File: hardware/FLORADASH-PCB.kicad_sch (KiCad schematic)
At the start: 45 parts, among them IC1 LM66200DRLR, J1 USB_C_Receptacle_USB2.0_16P, Q1 FS8205, Q2 FS8205, U1 ESP32-C3-WROOM-02, U2 TP4056-42-ESOP8, U3 USBLC6-2SC6, U5 MAX17048G_T10, U6 DW01A

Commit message: Added the DHT11 Module
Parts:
- added U7: DHT11, Connector_PinSocket_2.54mm:PinSocket_1x03_P2.54mm_Vertical, symbol DHT11_Board:DHT11_Board
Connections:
- net +3.3V: now also U7.2 (VCC)
- net GND: now also U7.3 (GND)

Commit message: New labels
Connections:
- net B+ is gone; now on net Bat+: BT1.1 (+), C4.1, IC1.6 (VIN2), R9.1, TP5.1, U2.5 (BAT)
- net B_Or_USB is gone; now on net battery/usb: IC1.2 (VOUT@1), IC1.7 (VOUT@2), TP3.1
- net B- renamed Bat-
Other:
- note added: "Sensor Humidity / Temperature"
- moved on the sheet: BT1, C3, C4, C9, D3, Q1, Q2, R10, R5, R6, R9, TP5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

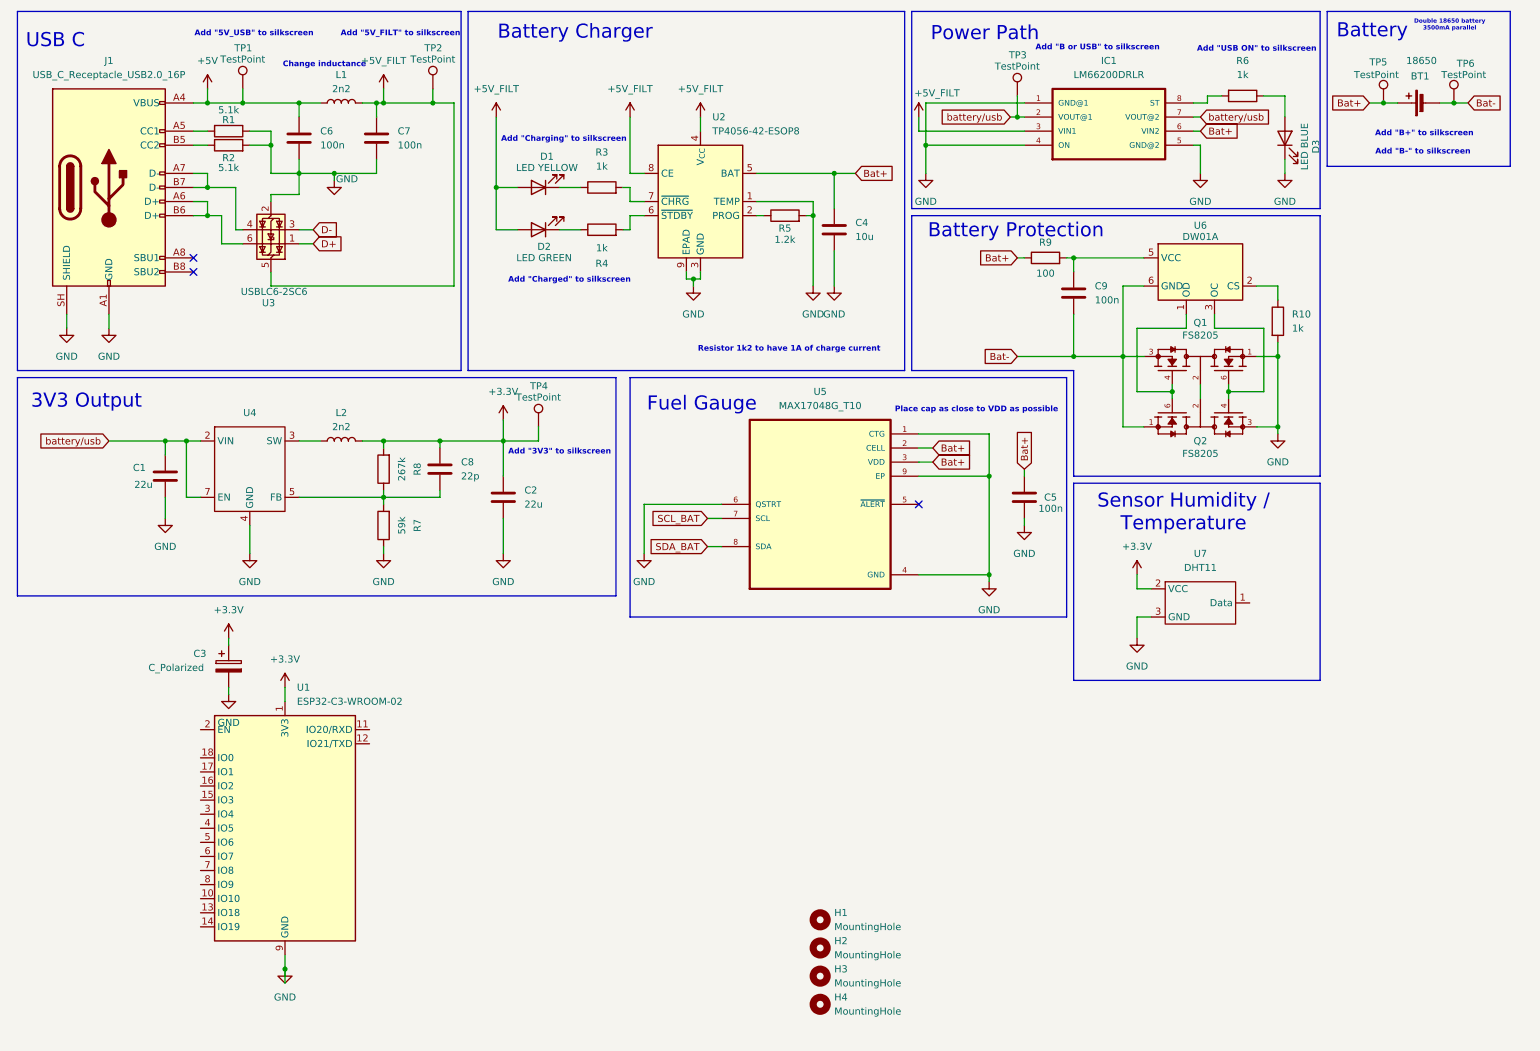
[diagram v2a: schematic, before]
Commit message: Added the Soil Moisture Sensor and LDR Sensor
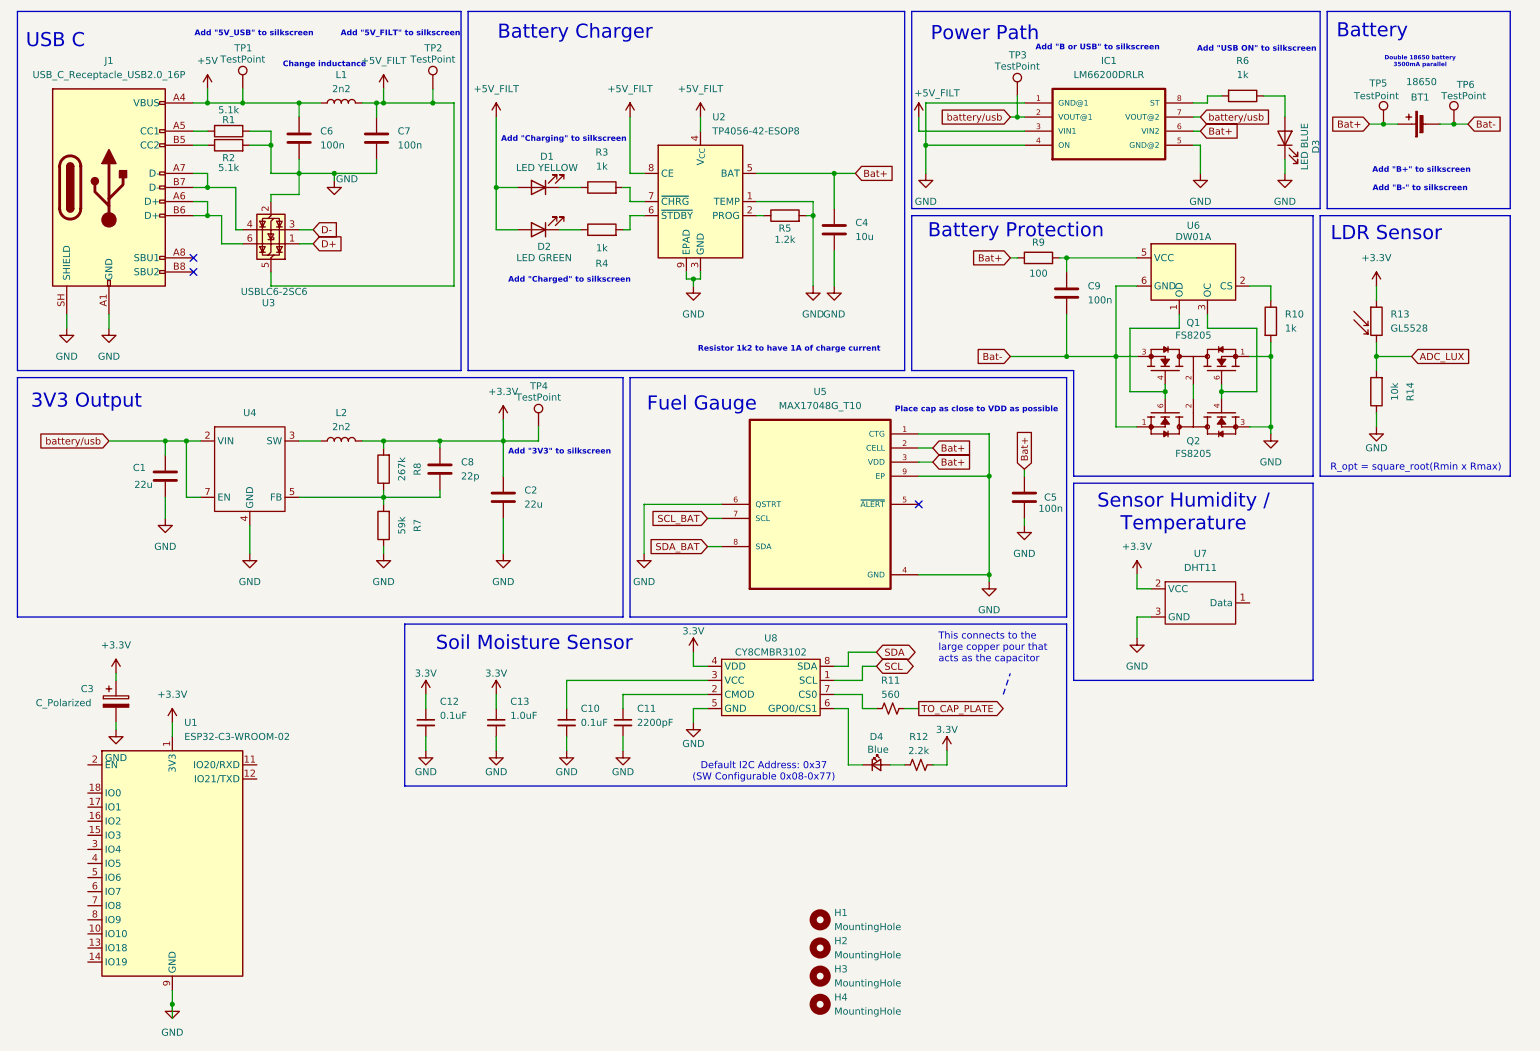
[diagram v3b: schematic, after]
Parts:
- added C10, C12: 0.1uF, SparkFun-Capacitor:C_0603_1608Metric, symbol SparkFun-Capacitor:0.1uF_0603_25V_20%
- added C11: 2200pF, SparkFun-Capacitor:C_0603_1608Metric, symbol SparkFun-Capacitor:2200pF_0603_50V_10%
- added C13: 1.0uF, SparkFun-Capacitor:C_0603_1608Metric, symbol SparkFun-Capacitor:1.0uF_0603_16V_10%
- added D4: Blue, SparkFun-LED:LED_0603_1608Metric_Blue, symbol SparkFun-LED:LED_Blue_0603
- added R11: 560, SparkFun-Resistor:R_0603_1608Metric, symbol SparkFun-Resistor:560_0603
- added R12: 2.2k, SparkFun-Resistor:R_0603_1608Metric, symbol SparkFun-Resistor:2.2k_0603
- added R13: GL5528, Connector_PinSocket_2.00mm:PinSocket_1x02_P2.00mm_Vertical, symbol Device:R_Photo
- added R14: 10k, symbol Device:R
- added U8: CY8CMBR3102, SparkFun-Semiconductor-Standard:SO-8, symbol SparkFun-Sensor:CY8CMBR3102
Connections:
- net +3.3V: now also R13.1
- net GND: now also C10.2, C11.2, C12.2, C13.2, R14.1, U8.5 (GND)
- new net: C11.1, U8.2 (CMOD)
- new net: C10.1, U8.3 (VCC)
- new net: D4.1 (K), U8.6 (GPO0/CS1)
- new net: R11.1, U8.7 (CS0)
- new net: D4.2 (A), R12.2
- new net 3.3V: C12.1, C13.1, R12.1, U8.4 (VDD)
- new net ADC_LUX: R13.2, R14.2
- new net SCL: U8.1 (SCL)
- new net SDA: U8.8 (SDA)
- new net TO_CAP_PLATE: R11.2
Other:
- note added: "Default I2C Address: 0x37 (SW Configurable 0x08-0x77)"
- note added: "LDR Sensor"
- note added: "R_opt = square_root(Rmin x Rmax)"
- note added: "Soil Moisture Sensor"
- note added: "This connects to the large copper pour that acts as the capacitor"
- moved on the sheet: BT1, C3, C9, Q1, Q2, R10, R9, TP5, TP6, U1, U6

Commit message: Added the Switch and low pass filter
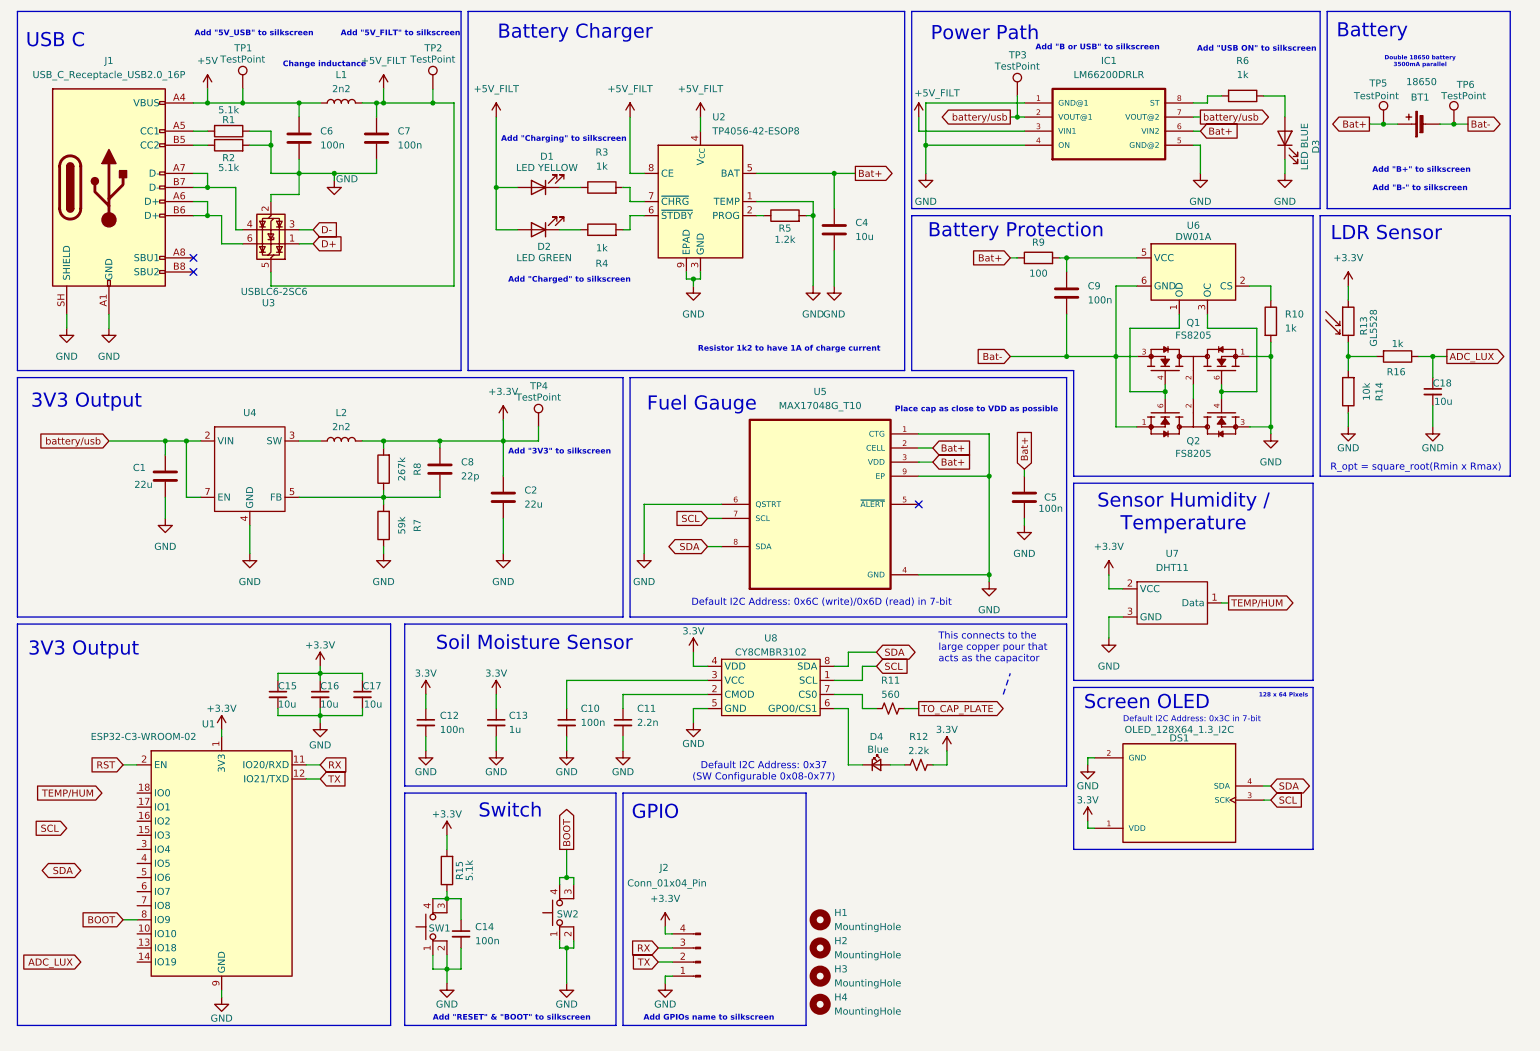
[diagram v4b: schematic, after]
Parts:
- removed C3: C_Polarized, symbol Device:C_Polarized
- added C14: 100n, SparkFun-Capacitor:C_0603_1608Metric, symbol SparkFun-Capacitor:0.1uF_0603_25V_20%
- added C15, C16, C17, C18: 10u, SparkFun-Capacitor:C_0603_1608Metric, symbol SparkFun-Capacitor:1.0uF_0603_16V_10%
- added DS1: OLED_128X64_1.3_I2C, OLED_128X64_1.3_I2C:LCD_OLED_128X64_1.3_I2C, symbol OLED_128X64_1.3_I2C:OLED_128X64_1.3_I2C
- added J2: Conn_01x04_Pin, symbol Connector:Conn_01x04_Pin
- added R15: 5.1k, symbol Device:R
- added R16: 1k, symbol Device:R
- added SW1: RESET, symbol Switch:SW_MEC_5E
- added SW2: BOOT, symbol Switch:SW_MEC_5E
- C10, C12: value 0.1uF -> 100n
- C11: value 2200pF -> 2.2n
- C13: value 1.0uF -> 1u
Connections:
- net SCL_BAT is gone; now on net SCL: U5.7 (SCL)
- net SDA_BAT is gone; now on net SDA: U5.8 (SDA)
- net +3.3V: now also C15.1, C16.1, C17.1, J2.4 (Pin_4), R15.2
- net 3.3V: now also DS1.1 (VDD)
- net ADC_LUX: now also C18.1, R16.1; no longer R13.2, R14.2
- net GND: now also C14.2, C15.2, C16.2, C17.2, C18.2, DS1.2 (GND), J2.1 (Pin_1), SW1.1, SW1.2, SW2.1, SW2.2
- net SCL: now also DS1.3 (SCK)
- net SDA: now also DS1.4 (SDA)
- net TEMP/HUM: now reaches U7.1 (Data)
- net RX: now reaches U1.11 (IO20/RXD)
- net RX: now also J2.3 (Pin_3)
- net TX: now reaches U1.12 (IO21/TXD)
- net TX: now also J2.2 (Pin_2)
- net RST: now reaches U1.2 (EN)
- net BOOT: now reaches U1.8 (IO9)
- net BOOT: now also SW2.3 (K), SW2.4 (A)
- new net: C14.1, R15.1, SW1.3 (K), SW1.4 (A)
- new net: R13.2, R14.2, R16.2
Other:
- note added: "128 x 64 Pixels"
- note added: "Add "RESET" & "BOOT" to silkscreen"
- note added: "Add GPIOs name to silkscreen"
- note added: "Default I2C Address: 0x3C in 7-bit"
- note added: "Default I2C Address: 0x6C (write)/0x6D (read) in 7-bit"
- note added: "GPIO"
- note added: "Screen OLED"
- note added: "Switch"
- moved on the sheet: R13, R14, U1, U7

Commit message: Added the pull-up I2C and logo
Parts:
- added R17, R18: 4.7k, symbol Device:R
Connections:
- net +3.3V: now also R17.1, R18.1
- net SCL: now also R17.2
- net SDA: now also R18.2
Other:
- company: Personal -> Stanley Selvaratnam

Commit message: Clean up schema
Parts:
- removed D4: Blue, SparkFun-LED:LED_0603_1608Metric_Blue, symbol SparkFun-LED:LED_Blue_0603
- removed R11: 560, SparkFun-Resistor:R_0603_1608Metric, symbol SparkFun-Resistor:560_0603
- removed R12: 2.2k, SparkFun-Resistor:R_0603_1608Metric, symbol SparkFun-Resistor:2.2k_0603
- added D4: LED BLUE, Diode_SMD:D_0603_1608Metric, symbol Device:LED
- added D5: LED YELLOW, Diode_SMD:D_0603_1608Metric, symbol Device:LED
- added J3: Conn_01x05_Pin, Connector_PinSocket_2.54mm:PinSocket_1x05_P2.54mm_Vertical, symbol Connector:Conn_01x05_Pin
- added R11: 560, Resistor_SMD:R_0603_1608Metric, symbol Device:R
- added R12: 2.2k, Resistor_SMD:R_0603_1608Metric, symbol Device:R
- added R19: 1k, Resistor_SMD:R_0603_1608Metric, symbol Device:R
- BT1: footprint Connector_JST:JST_ACH_BM02B-ACHSS-GAN-ETF_1x02-1MP_P1.20mm_Vertical -> (none); JLCPCB Part # (none) -> C6937126
- C1, C2, C4, C5, C6, C7, C8, C9: footprint (none) -> Capacitor_SMD:C_0603_1608Metric
- C10, C11, C12, C13, C14, C15, C16, C17, C18: footprint SparkFun-Capacitor:C_0603_1608Metric -> Capacitor_SMD:C_0603_1608Metric
- D1: value LED YELLOW -> LED RED; footprint (none) -> Diode_SMD:D_0603_1608Metric; JLCPCB Part # (none) -> C2286
- D2: footprint (none) -> Diode_SMD:D_0603_1608Metric; JLCPCB Part # (none) -> C12624
- D3: footprint (none) -> Diode_SMD:D_0603_1608Metric; JLCPCB Part # (none) -> C2288
- DS1, U7: now left out of the parts list
- IC1: JLCPCB Part # (none) -> C3235556
- J1: footprint Connector_USB:USB_C_Receptacle_Amphenol_12401948E412A -> Connector_USB:USB_C_Receptacle_G-Switch_GT-USB-7010ASV; JLCPCB Part # (none) -> C2765186
- J2: footprint (none) -> Connector_PinSocket_2.54mm:PinSocket_1x04_P2.54mm_Vertical
- Q1, Q2: JLCPCB Part # (none) -> C908265
- R1, R10, R14, R15, R16, R17, R18, R2, R3, R4, R5, R6, R7, R8, R9: footprint (none) -> Resistor_SMD:R_0603_1608Metric
- SW1, SW2: footprint (none) -> Button_Switch_SMD:SW_Push_1P1T_XKB_TS-1187A; JLCPCB Part # (none) -> C318884
- TP1, TP2, TP3, TP4, TP5, TP6: footprint (none) -> TestPoint:TestPoint_Pad_D2.5mm
- U1: JLCPCB Part # (none) -> C2934560
- U2: JLCPCB Part # (none) -> C16581
- U3: JLCPCB Part # (none) -> C7519
- U4: value (none) -> MT3420SP; footprint (none) -> Package_SO:SOIC-8_3.9x4.9mm_P1.27mm; JLCPCB Part # (none) -> C88265
- U5: JLCPCB Part # (none) -> C2682616
- U6: JLCPCB Part # (none) -> C351410
- U8: footprint SparkFun-Semiconductor-Standard:SO-8 -> Package_SO:SOIC-8_3.9x4.9mm_P1.27mm; JLCPCB Part # (none) -> C2759924
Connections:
- net +5V: now also U3.2 (GND)
- net +5V_FILT: no longer U3.5 (VBUS)
- net 3.3V: now also R12.2
- net ADC_LUX: now also U1.18 (IO0)
- net D+: now also U1.14 (IO19), U3.6 (I/O1); no longer U3.1 (I/O1)
- net D-: now also U1.13 (IO18), U3.4 (I/O2); no longer U3.3 (I/O2)
- net GND: now also U3.5 (VBUS), D5.1 (K); no longer U3.2 (GND)
- net RST: now also C14.1, R15.1, SW1.3 (K), SW1.4 (A)
- net SCL: now also U1.17 (IO1)
- net SDA: now also U1.16 (IO2)
- net TEMP/HUM: now also U1.15 (IO3)
- net TO_CAP_PLATE: now also R11.2
- net at U8.6 (GPO0/CS1): now also D4.1 (K)
- net at U8.7 (CS0): now also R11.1
- net at J1.A7 (D-), J1.B7 (D-): now also U3.3 (I/O2); no longer U3.4 (I/O2)
- net at J1.A6 (D+), J1.B6 (D+): now also U3.1 (I/O1); no longer U3.6 (I/O1)
- net GPIO10: now reaches U1.10 (IO10)
- net GPIO10: now also J3.1 (Pin_1)
- net at U1.3 (IO4): now also R19.2
- net GPIO5: now reaches U1.4 (IO5)
- net GPIO5: now also J3.5 (Pin_5)
- net GPIO6: now reaches U1.5 (IO6)
- net GPIO6: now also J3.4 (Pin_4)
- net GPIO7: now reaches U1.6 (IO7)
- net GPIO7: now also J3.3 (Pin_3)
- net GPIO8: now reaches U1.7 (IO8)
- net GPIO8: now also J3.2 (Pin_2)
- new net: D4.2 (A), R12.1
- new net: D5.2 (A), R19.1
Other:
- note added: "Differential pair"
- note added: "ESP32"
- note added: "I2C Addr : 0x3C in 7bit"
- note removed: "Default I2C Address: 0x3C in 7-bit"
- company: Stanley Selvaratnam -> (none)

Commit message: Clean up the GPIOs add TVS protection
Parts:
- removed J3: Conn_01x05_Pin, Connector_PinSocket_2.54mm:PinSocket_1x05_P2.54mm_Vertical, symbol Connector:Conn_01x05_Pin
- added C19, C20: 100n, Capacitor_SMD:C_0603_1608Metric, symbol SparkFun-Capacitor:0.1uF_0603_25V_20%
- added J3: Conn_02x04_Top_Bottom, Connector_PinHeader_1.00mm:PinHeader_2x04_P1.00mm_Vertical, symbol Connector_Generic:Conn_02x04_Top_Bottom
- added R20, R21: 47, Resistor_SMD:R_0603_1608Metric, symbol Device:R
- added U9: USBLC6-2SC6, Package_TO_SOT_SMD:SOT-23-6, symbol Power_Protection:USBLC6-2SC6
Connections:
- net +3.3V: now also J3.1 (Pin_1), U9.5 (VBUS)
- net +5V: now also U3.5 (VBUS); no longer U3.2 (GND)
- net 3.3V: now also C19.1, C20.1
- net D+: now also U3.4 (I/O2); no longer U3.6 (I/O1)
- net D-: now also U3.6 (I/O1); no longer U3.4 (I/O2)
- net GND: now also U3.2 (GND), C19.2, C20.2, J3.4 (Pin_4), J3.8 (Pin_8), U9.2 (GND); no longer U3.5 (VBUS)
- net GPIO10: now also J3.7 (Pin_7)
- net GPIO5: now also J3.2 (Pin_2)
- net GPIO6: now also J3.3 (Pin_3)
- net GPIO7: now also J3.5 (Pin_5)
- net GPIO8: now also J3.6 (Pin_6)
- net RX: now also R20.2, U9.1 (I/O1); no longer J2.3 (Pin_3), U1.11 (IO20/RXD)
- net TX: now also R21.2, U9.3 (I/O2); no longer J2.2 (Pin_2), U1.12 (IO21/TXD)
- net at J1.A6 (D+), J1.B6 (D+): now also U3.3 (I/O2); no longer U3.1 (I/O1)
- net at J1.A7 (D-), J1.B7 (D-): now also U3.1 (I/O1); no longer U3.3 (I/O2)
- new net: R21.1, U1.12 (IO21/TXD)
- new net: J2.2 (Pin_2), U9.4 (I/O2)
- new net: J2.3 (Pin_3), U9.6 (I/O1)
- new net: R20.1, U1.11 (IO20/RXD)
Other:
- note added: "Hole"

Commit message: Started the PCB and rules
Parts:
- removed BT1: 18650, symbol Device:Battery_Cell
- removed C10, C12, C14, C19, C20: 100n, Capacitor_SMD:C_0603_1608Metric, symbol SparkFun-Capacitor:0.1uF_0603_25V_20%
- removed C11: 2.2n, Capacitor_SMD:C_0603_1608Metric, symbol SparkFun-Capacitor:2200pF_0603_50V_10%
- removed C13: 1u, Capacitor_SMD:C_0603_1608Metric, symbol SparkFun-Capacitor:1.0uF_0603_16V_10%
- removed C15, C16, C17, C18: 10u, Capacitor_SMD:C_0603_1608Metric, symbol SparkFun-Capacitor:1.0uF_0603_16V_10%
- removed SW1: RESET, Button_Switch_SMD:SW_Push_1P1T_XKB_TS-1187A, symbol Switch:SW_MEC_5E
- removed SW2: BOOT, Button_Switch_SMD:SW_Push_1P1T_XKB_TS-1187A, symbol Switch:SW_MEC_5E
- removed U8: CY8CMBR3102, Package_SO:SOIC-8_3.9x4.9mm_P1.27mm, symbol SparkFun-Sensor:CY8CMBR3102
- added BT1: (no value), 2-18650:BAT-SMD_BH-18650-B1BA007, symbol 18650:2-CELL-18650
- added C10, C11, C12: 22u, Capacitor_SMD:C_0603_1608Metric, symbol Device:C
- added C13, C15, C17, C18, C19, C5: 100n, Capacitor_SMD:C_0603_1608Metric, symbol Device:C
- added C14: 1u, Capacitor_SMD:C_0603_1608Metric, symbol Device:C
- added C16: 2n2, Capacitor_SMD:C_0603_1608Metric, symbol Device:C
- added SW1, SW2: SW_Push, Button_Switch_SMD:SW_Push_1P1T_XKB_TS-1187A, symbol Switch:SW_Push
- added U7: CY8CMBR3102, Package_SO:JEITA_SOIC-8_3.9x4.9mm_P1.27mm, symbol CY8CMBR3102:CY8CMBR3102
- H1, H4: footprint (none) -> MountingHole:MountingHole_2.2mm_M2_DIN965_Pad
- H2: renamed from H3; footprint (none) -> MountingHole:MountingHole_2.2mm_M2_DIN965_Pad
- H3: renamed from H2; footprint (none) -> MountingHole:MountingHole_2.2mm_M2_DIN965_Pad
- J3: footprint Connector_PinHeader_1.00mm:PinHeader_2x04_P1.00mm_Vertical -> Connector_PinHeader_2.54mm:PinHeader_2x04_P2.54mm_Vertical
- L2: value 2n2 -> 2u2
- renumbered C6 to C1, C7 to C2, C4 to C3, C9 to C4, C8 to C6, C1 to C7, C2 to C8, C5 to C9, D3 to D1, D1 to D2, D2 to D3, R6 to R1, R16 to R10, R14 to R11, R8 to R12, R7 to R13, R11 to R14, R20 to R15, R12 to R16, R21 to R17, R19 to R18, R15 to R19, R1 to R2, R17 to R20, R18 to R21, R2 to R3, R3 to R4, R4 to R6, R9 to R7, R10 to R8, R13 to R9, TP5 to TP4, TP6 to TP5, TP4 to TP6, U2 to U1, U3 to U2, U6 to U3, U7 to U6, U1 to U8
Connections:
- net 3.3V is gone; now on net +3.3V: DS1.1 (VDD), R16.2
- net +3.3V: now also C10.1, C11.1, C12.1, C13.1, C14.1, C17.1, C18.1, U7.4 (VDD)
- net ADC_LUX: now also C5.1
- net BOOT: now also SW1.2
- net Bat+: now also BT1.1, BT1.3
- net Bat-: now also BT1.2, BT1.4
- net GND: now also C10.2, C11.2, C12.2, C13.2, C14.2, C15.2, C16.2, C17.2, C18.2, C19.2, C5.2, SW1.1, SW2.1, U7.5 (GND)
- net RST: now also C19.1, SW2.2
- net SCL: now also U7.1 (SCL)
- net SDA: now also U7.8 (SDA)
- net at D4.1 (K): now also U7.6 (GPO0/CS1)
- net at R14.1: now also U7.7 (CS0)
- new net: C16.1, U7.2 (CMOD)
- new net: C15.1, U7.3 (VCC)
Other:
- note added: "Hole M2"
- note removed: "Hole"
